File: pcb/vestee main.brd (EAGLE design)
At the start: 57.4 x 63.6 mm, 46 parts, among them IC1 LD117AS12TR, IC3 CP210X_USB_UART, Q1 MMBT2222A, Q3 MMBT2222A

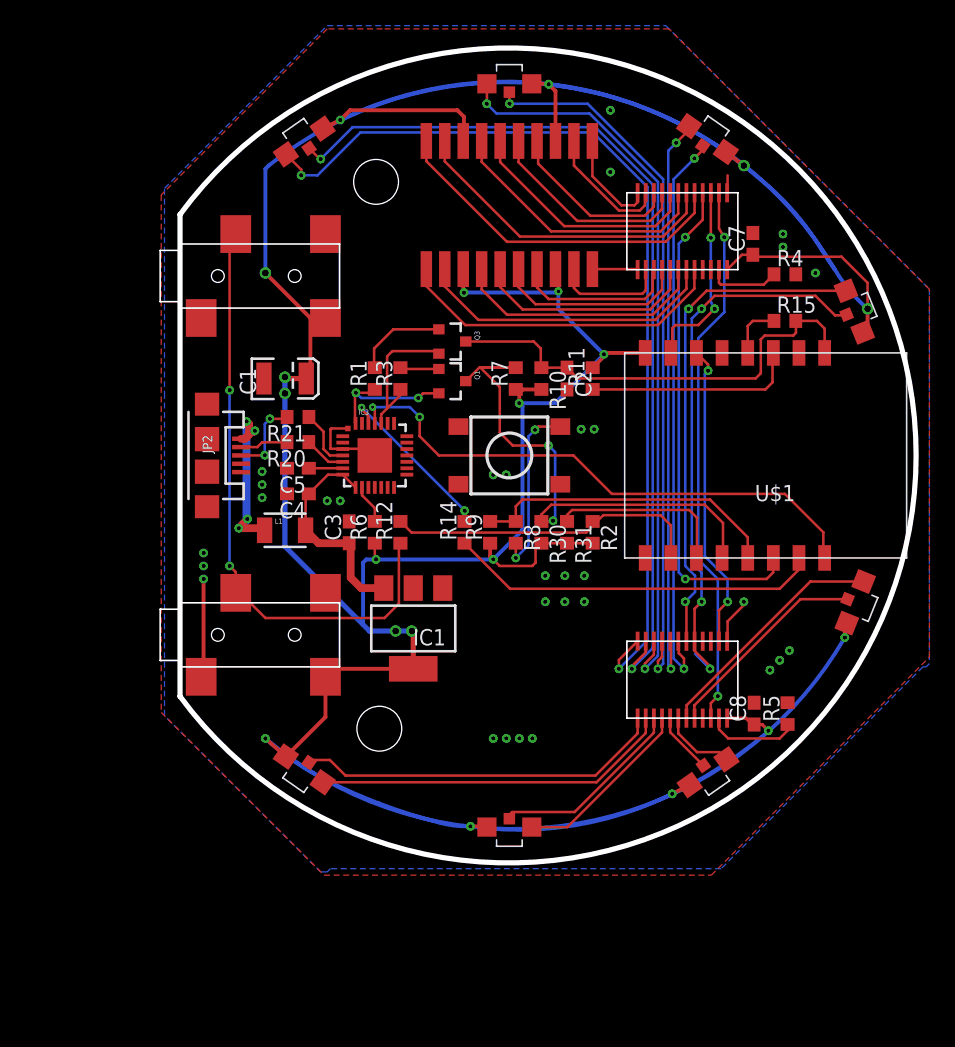
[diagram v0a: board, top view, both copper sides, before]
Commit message: Rerouted bottom traces to be covered by soldermask
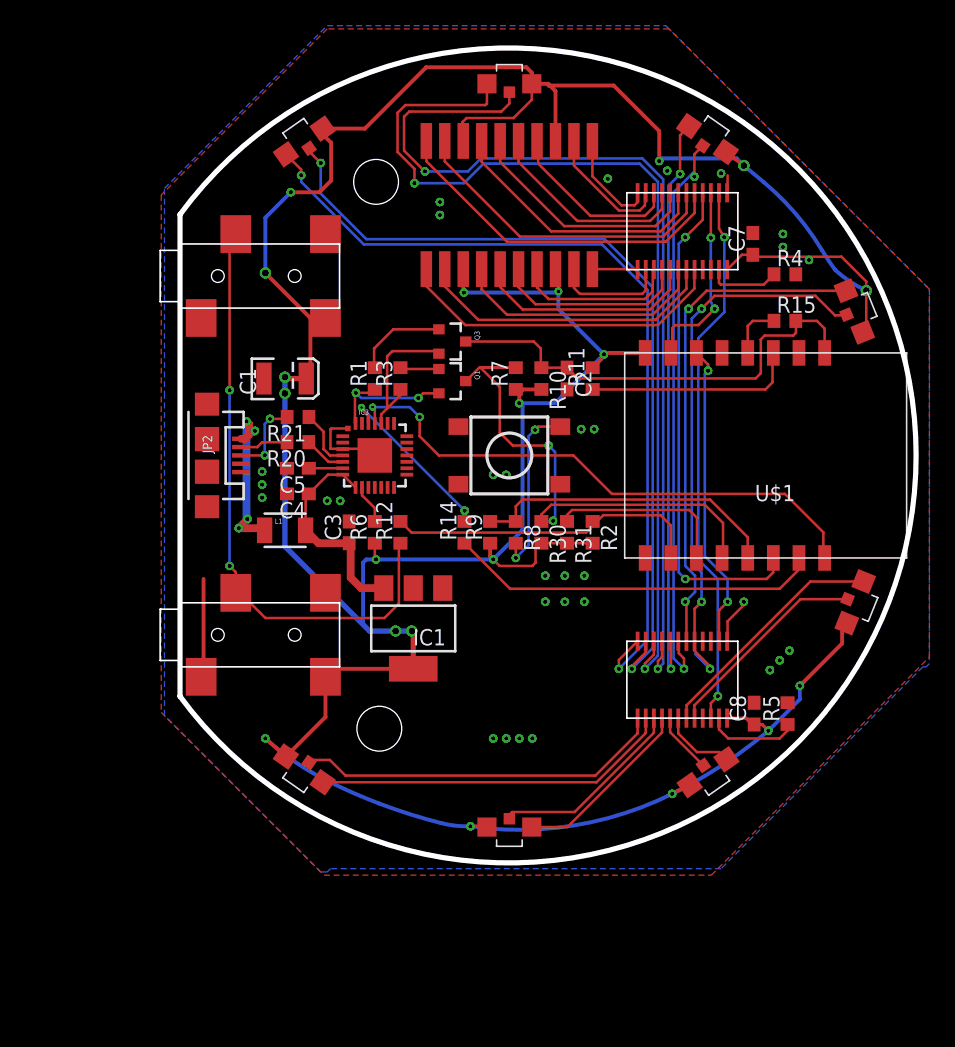
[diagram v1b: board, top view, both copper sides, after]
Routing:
- net VCC: track 384.9 -> 295.4 mm
- net D2R: track 56.0 -> 74.8 mm
- net D2G: track 58.3 -> 75.9 mm
- net D1G: track 73.6 -> 66.4 mm
- net D1R: track 71.1 -> 65.9 mm
- net D3R: track 44.4 -> 45.3 mm

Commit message: PCB conversion
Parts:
- added R13, R16: (no value), rcl:M1206
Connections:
- new net N$6: PRPIHERALS.2, R13.1
- new net N$8: PRPIHERALS1.2, R16.1
- net CLK: now also U$4.3
- net GND: now also U$3.21, U$4.21
- net LA/: now also U$4.4
- net VCC: now also R13.2, R16.2; no longer PRPIHERALS.2, PRPIHERALS1.2
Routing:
- net VCC: track 295.4 -> 289.1 mm
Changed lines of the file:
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@@
 <?xml version="1.0" encoding="utf-8"?>
 <!DOCTYPE eagle SYSTEM "eagle.dtd">
-<eagle version="7.4.0">
+<eagle version="7.5.0">
 <drawing>
 <settings>
@@
 <layer number="155" name="FabDoc3" color="7" fill="1" visible="yes" active="yes"/>
 <layer number="199" name="Contour" color="7" fill="1" visible="yes" active="yes"/>
-<layer number="200" name="200bmp" color="15" fill="0" visible="no" active="yes"/>
+<layer number="200" name="200bmp" color="15" fill="0" visible="yes" active="yes"/>
 <layer number="201" name="201bmp" color="2" fill="10" visible="yes" active="yes"/>
 <layer number="202" name="202bmp" color="3" fill="10" visible="yes" active="yes"/>
@@
 <element name="R4" library="rcl" package="R0603" value="" x="54.002" y="46.632"/>
 <element name="R5" library="rcl" package="R0603" value="" x="54.21" y="12.356" rot="R90"/>
+<element name="R13" library="rcl" package="M1206" value="" x="-3.048" y="-6.096"/>
+<element name="R16" library="rcl" package="M1206" value="" x="-3.048" y="-10.668"/>
 </elements>
 <signals>
@@
 <via x="49.022" y="54.5084" extent="1-16" drill="0.3048" shape="octagon"/>
 <via x="44.8184" y="54.716" extent="1-16" drill="0.3048" shape="octagon"/>
+<contactref element="U$3" pad="21"/>
+<contactref element="U$4" pad="21"/>
+<wire x1="51.5" y1="49.858" x2="47.5875" y2="47" width="0" layer="19" extent="1-1"/>
+<wire x1="47.5875" y1="12" x2="51.6" y2="13.202" width="0" layer="19" extent="1-1"/>
 </signal>
 <signal name="VCC">
@@
 <contactref element="R9" pad="1"/>
 <wire x1="43.1" y1="40.5" x2="42.81" y2="41.32" width="0.4064" layer="1"/>
-<contactref element="PRPIHERALS1" pad="2"/>
 <contactref element="C1" pad="A"/>
 <contactref element="R7" pad="1"/>
@@
 <contactref element="D2" pad="COM"/>
 <contactref element="D3" pad="COM"/>
-<contactref element="R6" pad="1"/>
 <contactref element="U$2" pad="18"/>
 <contactref element="U$2" pad="3"/>
 <contactref element="U$2" pad="13"/>
 <contactref element="U$2" pad="8"/>
-<contactref element="PRPIHERALS" pad="2"/>
 <via x="13.462" y="46.736" extent="1-16" drill="0.508" shape="octagon"/>
 <wire x1="13.462" y1="51.054" x2="13.462" y2="46.736" width="0.3048" layer="16"/>
 <wire x1="13.462" y1="46.736" x2="16.973" y2="43.225" width="0.3048" layer="1"/>
-<wire x1="16.973" y1="43.225" x2="18.15" y2="43.225" width="0.3048" layer="1"/>
 <wire x1="16.973" y1="43.225" x2="16.973" y2="38.823" width="0.3048" layer="1"/>
 <wire x1="16.973" y1="38.823" x2="16.65" y2="38.5" width="0.3048" layer="1"/>
@@
 <wire x1="56.896" y1="48.514" x2="57.912" y2="46.99" width="0.3048" layer="16" curve="5.36382"/>
 <wire x1="25" y1="15.85" x2="18.775" y2="15.85" width="0.3048" layer="1"/>
-<wire x1="18.775" y1="15.85" x2="18.15" y2="15.225" width="0.3048" layer="1"/>
-<wire x1="18.15" y1="15.225" x2="18.15" y2="12.087275" width="0.3048" layer="1"/>
 <wire x1="18.15" y1="12.087275" x2="15.06648125" y2="9.00375625" width="0.3048" layer="1"/>
 <wire x1="25" y1="15.85" x2="25" y2="18.688" width="0.4064" layer="1"/>
@@
 <wire x1="36.1" y1="57.04" x2="36.068" y2="57.072" width="0.3048" layer="1"/>
 <wire x1="28.9" y1="57.04" x2="28.956" y2="57.096" width="0.3048" layer="1"/>
-<wire x1="22" y1="25.65" x2="22" y2="24.482" width="0.2032" layer="1"/>
 <wire x1="22" y1="24.482" x2="22.098" y2="24.384" width="0.2032" layer="1"/>
 <via x="22.098" y="24.384" extent="1-16" drill="0.3048" shape="octagon"/>
@@
 <wire x1="44.3992" y1="55.6768" x2="50.2412" y2="55.6768" width="0.3048" layer="16"/>
 <wire x1="50.2412" y1="55.6768" x2="50.8" y2="55.118" width="0.3048" layer="16"/>
+<contactref element="R13" pad="2"/>
+<contactref element="R16" pad="2"/>
+<contactref element="R6" pad="1"/>
+<wire x1="22" y1="24.482" x2="22" y2="25.65" width="0" layer="19" extent="1-1"/>
+<wire x1="18.15" y1="12.087275" x2="18.775" y2="15.85" width="0" layer="19" extent="1-1"/>
+<wire x1="-1.648" y1="-6.096" x2="13.462" y2="10.414" width="0" layer="19" extent="1-16"/>
+<wire x1="-1.648" y1="-10.668" x2="-1.648" y2="-6.096" width="0" layer="19" extent="1-1"/>
 </signal>
 <signal name="1-WIRE">
@@
 <wire x1="45.212" y1="42.418" x2="45.212" y2="40.612" width="0.2032" layer="1"/>
 <wire x1="45.212" y1="40.612" x2="45.1" y2="40.5" width="0.2032" layer="1"/>
+<contactref element="U$4" pad="3"/>
+<wire x1="48.2225" y1="18" x2="45.1" y2="40.5" width="0" layer="19" extent="1-1"/>
 </signal>
 <signal name="LA/">
@@
 <wire x1="53.086" y1="23.368" x2="53.086" y2="24.486" width="0.2032" layer="1"/>
 <wire x1="53.086" y1="24.486" x2="53.1" y2="24.5" width="0.2032" layer="1"/>
+<contactref element="U$4" pad="4"/>
+<wire x1="47.5875" y1="18" x2="46.228" y2="22.86" width="0" layer="19" extent="1-16"/>
 </signal>
 <signal name="REST">
@@
 <wire x1="54.21" y1="11.03" x2="54.21" y2="11.506" width="0.2032" layer="1"/>
 </signal>
+<signal name="N$6">
+<contactref element="PRPIHERALS" pad="2"/>
+<contactref element="R13" pad="1"/>
+<wire x1="-4.448" y1="-6.096" x2="18.15" y2="43.225" width="0" layer="19" extent="1-1"/>
+</signal>
+<signal name="N$8">
+<contactref element="PRPIHERALS1" pad="2"/>
+<contactref element="R16" pad="1"/>
+<wire x1="-4.448" y1="-10.668" x2="18.15" y2="15.225" width="0" layer="19" extent="1-1"/>
+</signal>
 </signals>

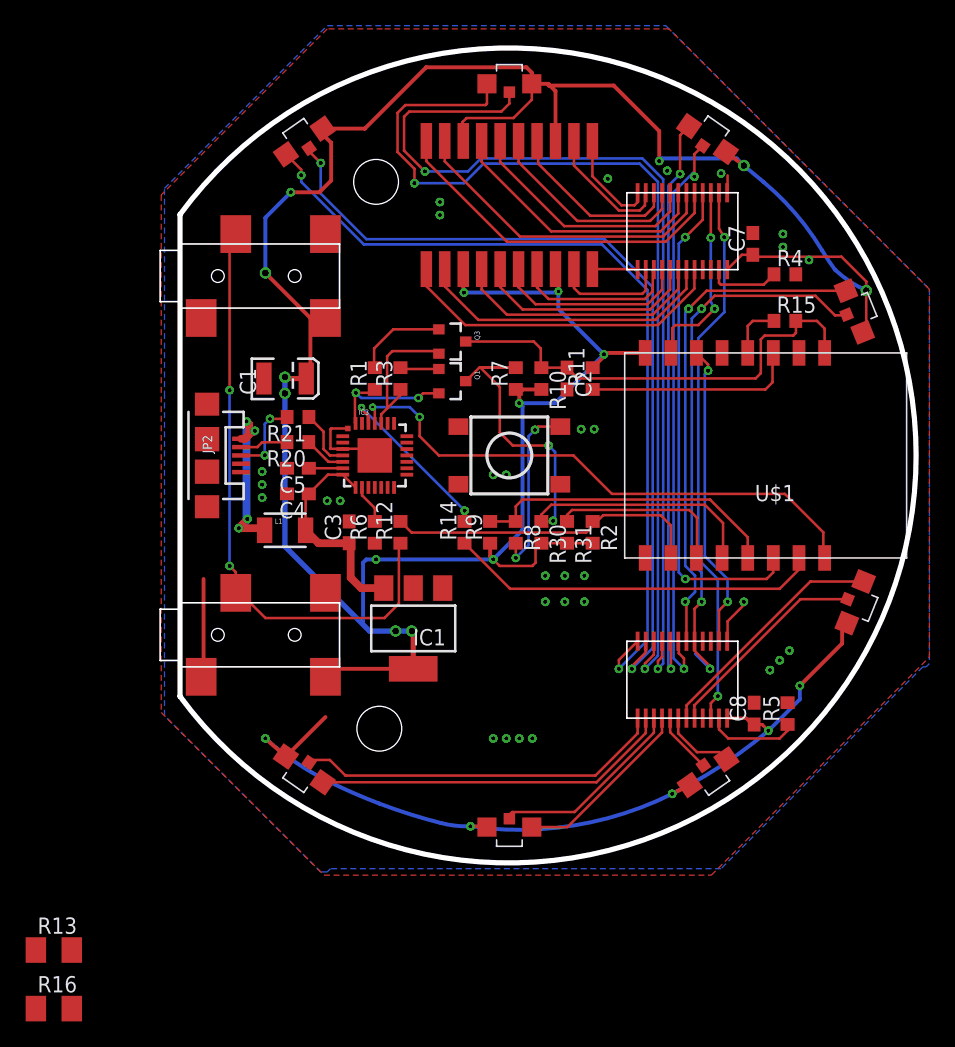
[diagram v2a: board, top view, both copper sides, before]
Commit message: Layout adjusted to schematic bug fixes
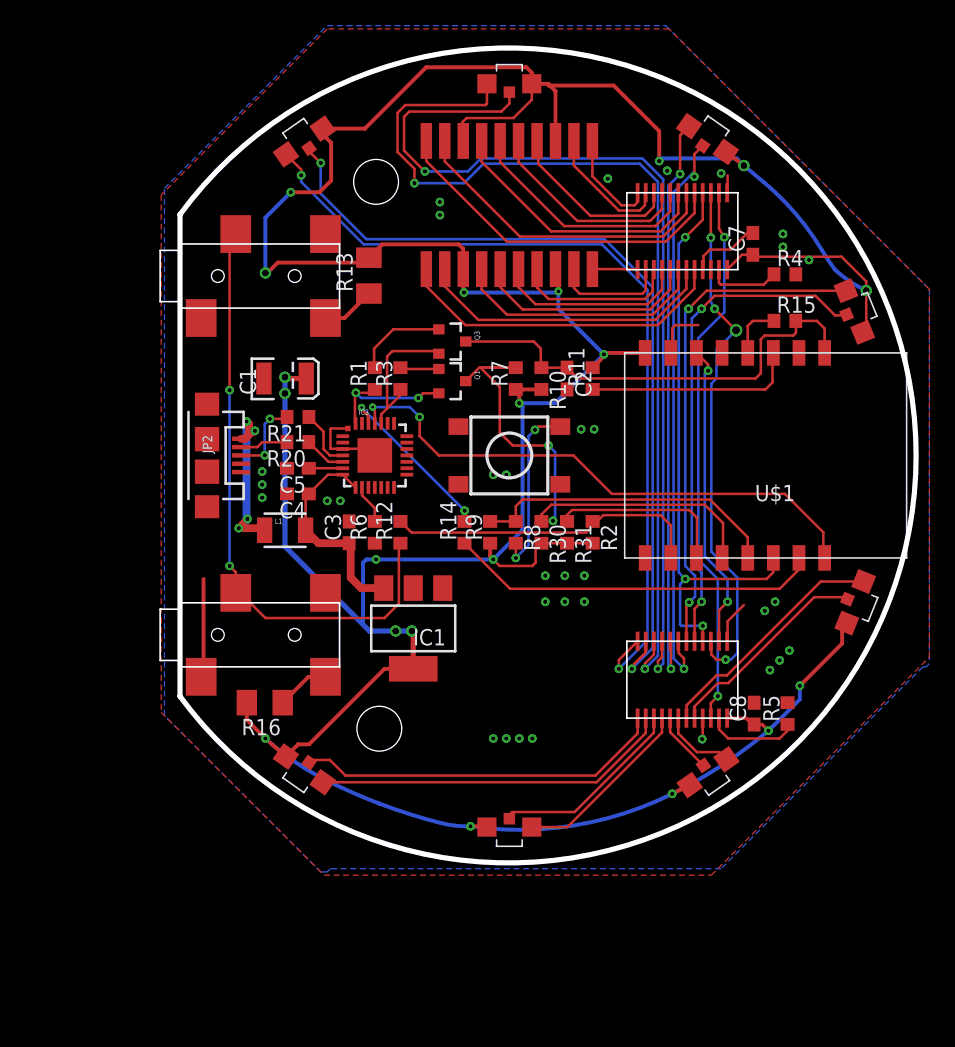
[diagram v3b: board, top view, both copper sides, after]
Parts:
- moved R13 58.1 mm to (21.5, 46.5), turned to 90 degrees
- moved R16 29.0 mm to (13.4, 13.2), turned to 180 degrees
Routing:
- net CLK: track 15.0 -> 45.9 mm, vias 2 -> 4
- net VCC: track 289.1 -> 303.4 mm
- net GND: track 19.4 -> 26.8 mm, vias 31 -> 33
- net LA/: track 39.3 -> 46.1 mm, vias 2 -> 3
- net D4R: track 43.5 -> 39.2 mm, vias 3 -> 2
- net N$6: track 0.00 -> 4.18 mm
- net N$8: track 0.00 -> 4.17 mm

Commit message: Fixes
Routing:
- net CLK: track 45.9 -> 48.9 mm, vias 4 -> 5
- net VCC: track 303.4 -> 304.5 mm
- net GND: vias 33 -> 38
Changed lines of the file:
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@@
 <wire x1="49.784" y1="48.5648" x2="51.0772" y2="49.858" width="0.2032" layer="1"/>
 <wire x1="51.0772" y1="49.858" x2="51.5" y2="49.858" width="0.2032" layer="1"/>
-<wire x1="47.5875" y1="47" x2="37" y2="37.65" width="0" layer="19" extent="1-1"/>
+<via x="48.6664" y="42.0624" extent="1-16" drill="0.3048" shape="octagon"/>
+<via x="41.2496" y="41.7576" extent="1-16" drill="0.3048" shape="octagon"/>
+<via x="40.3352" y="41.7576" extent="1-16" drill="0.3048" shape="octagon"/>
+<via x="37.084" y="41.7576" extent="1-16" drill="0.3048" shape="octagon"/>
+<via x="36.1696" y="41.7576" extent="1-16" drill="0.3048" shape="octagon"/>
 </signal>
 <signal name="VCC">
@@
 <wire x1="16.8656" y1="9.9568" x2="16.019525" y2="9.9568" width="0.3048" layer="1"/>
 <wire x1="16.019525" y1="9.9568" x2="15.06648125" y2="9.00375625" width="0.3048" layer="1"/>
-<wire x1="22" y1="24.482" x2="22" y2="25.65" width="0" layer="19" extent="1-1"/>
+<wire x1="22" y1="24.482" x2="22" y2="25.65" width="0.3048" layer="1"/>
 </signal>
 <signal name="1-WIRE">
@@
 <wire x1="48.2225" y1="44.4875" x2="48.514" y2="43.942" width="0.2032" layer="16"/>
 <via x="48.514" y="43.942" extent="1-16" drill="0.3048" shape="octagon"/>
-<wire x1="47.244" y1="42.672" x2="45.466" y2="42.672" width="0.2032" layer="1"/>
-<wire x1="45.466" y1="42.672" x2="45.212" y2="42.418" width="0.2032" layer="1"/>
-<wire x1="45.212" y1="42.418" x2="45.212" y2="40.612" width="0.2032" layer="1"/>
 <wire x1="45.212" y1="40.612" x2="45.1" y2="40.5" width="0.2032" layer="1"/>
 <contactref element="U$4" pad="3"/>
 <wire x1="48.514" y1="43.942" x2="50.1904" y2="42.2656" width="0.2032" layer="1"/>
-<via x="50.1904" y="42.2656" extent="1-16" drill="0.6" shape="square"/>
+<via x="50.1904" y="42.2656" extent="1-16" drill="0.3048" shape="octagon"/>
 <wire x1="50.1904" y1="42.2656" x2="48.6664" y2="40.7416" width="0.2032" layer="16"/>
 <wire x1="48.6664" y1="40.7416" x2="48.6664" y2="38.5064" width="0.2032" layer="16"/>
@@
 <wire x1="50.292" y1="17.0688" x2="49.784" y2="16.5608" width="0.2032" layer="16"/>
 <wire x1="49.784" y1="16.5608" x2="49.3776" y2="16.5608" width="0.2032" layer="16"/>
-<wire x1="48.514" y1="43.942" x2="47.244" y2="42.672" width="0" layer="19" extent="1-16"/>
+<wire x1="45.212" y1="40.612" x2="45.212" y2="39.2176" width="0.2032" layer="1"/>
+<wire x1="45.212" y1="39.2176" x2="45.9232" y2="38.5064" width="0.2032" layer="1"/>
+<via x="49.3776" y="38.9128" extent="1-16" drill="0.3048" shape="octagon"/>
+<wire x1="48.6664" y1="38.5064" x2="49.0728" y2="38.9128" width="0.2032" layer="16"/>
+<wire x1="49.0728" y1="38.9128" x2="49.3776" y2="38.9128" width="0.2032" layer="16"/>
+<wire x1="45.9232" y1="38.5064" x2="48.9712" y2="38.5064" width="0.2032" layer="1"/>
+<wire x1="48.9712" y1="38.5064" x2="49.3776" y2="38.9128" width="0.2032" layer="1"/>
 </signal>
 <signal name="LA/">
@@
 <wire x1="35" y1="39.35" x2="37" y2="39.35" width="0.2032" layer="1"/>
 <wire x1="37" y1="39.35" x2="37.84" y2="38.51" width="0.2032" layer="1"/>
-<wire x1="37.84" y1="38.51" x2="51.718" y2="38.51" width="0.2032" layer="1"/>
 <wire x1="52.4256" y1="41.8592" x2="54.6608" y2="41.8592" width="0.2032" layer="1"/>
 <wire x1="54.6608" y1="41.8592" x2="54.864" y2="42.0624" width="0.2032" layer="1"/>
@@
 <wire x1="52.4256" y1="41.8592" x2="52.12" y2="41.5536" width="0.2032" layer="1"/>
 <wire x1="52.12" y1="41.5536" x2="52.12" y2="38.912" width="0.2032" layer="1"/>
-<wire x1="52.12" y1="38.912" x2="51.718" y2="38.51" width="0.2032" layer="1"/>
 <wire x1="29.1" y1="41.3904" x2="34.4032" y2="41.3904" width="0.2032" layer="1"/>
 <wire x1="34.4032" y1="41.3904" x2="34.9504" y2="40.8432" width="0.2032" layer="1"/>
 <wire x1="34.9504" y1="40.8432" x2="34.9504" y2="39.3996" width="0.2032" layer="1"/>
 <wire x1="34.9504" y1="39.3996" x2="35" y2="39.35" width="0.2032" layer="1"/>
+<wire x1="52.12" y1="38.912" x2="51.308" y2="38.1" width="0.2032" layer="1"/>
+<wire x1="51.308" y1="38.1" x2="40.0304" y2="38.1" width="0.2032" layer="1"/>
+<wire x1="40.0304" y1="38.1" x2="39.6204" y2="38.51" width="0.2032" layer="1"/>
+<wire x1="39.6204" y1="38.51" x2="37.84" y2="38.51" width="0.2032" layer="1"/>
 </signal>
 <signal name="N$5">
